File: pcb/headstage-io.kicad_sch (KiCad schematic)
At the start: 3 parts, among them J2 BTE-040-03-L-D-A, J3 BTE-040-03-L-D-A

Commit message: 1st step OEPSPN & MPN on components
- still missing new codes to be emitted
- project/schematic/components not tunned with Jon's project at this date
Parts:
- J2, J3: MPN (none) -> BTE-040-03-L-D-A; OEPSPN (none) -> espera
- R288: MPN (none) -> RG1005P-104-B-T5; OEPSPN (none) -> OEPS020175
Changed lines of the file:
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@@
 			)
 		)
-		(property "Datasheet1" ""
+		(property "Tolerance" "0.1%"
 			(at 68.58 148.59 0)
 			(effects
@@
 			)
 		)
-		(property "Part No." ""
+		(property "MPN" "RG1005P-104-B-T5"
 			(at 68.58 148.59 0)
 			(effects
@@
 			)
 		)
-		(property "Tolerance" "0.1%"
+		(property "OEPSPN" "OEPS020175"
 			(at 68.58 148.59 0)
 			(effects
@@
 			)
 		)
-		(property "Datasheet1" ""
-			(at 194.31 92.71 0)
-			(effects
-				(font
-					(size 1.27 1.27)
-				)
-				(hide yes)
-			)
-		)
-		(property "Part No." ""
-			(at 194.31 92.71 0)
-			(effects
-				(font
-					(size 1.27 1.27)
-				)
-				(hide yes)
-			)
-		)
 		(property "Tolerance" ""
 			(at 194.31 92.71 0)
@@
 					(size 1.27 1.27)
 				)
+			)
+		)
+		(property "OEPSPN" "espera"
+			(at 194.31 92.71 0)
+			(effects
+				(font
+					(size 1.27 1.27)
+				)
+				(hide yes)
+			)
+		)
+		(property "MPN" "BTE-040-03-L-D-A"
+			(at 194.31 92.71 0)
+			(effects
+				(font
+					(size 1.27 1.27)
+				)
+				(hide yes)
 			)
 		)
@@
 			)
 		)
-		(property "Datasheet1" ""
-			(at 88.9 92.71 0)
-			(effects
-				(font
-					(size 1.27 1.27)
-				)
-				(hide yes)
-			)
-		)
-		(property "Part No." ""
-			(at 88.9 92.71 0)
-			(effects
-				(font
-					(size 1.27 1.27)
-				)
-				(hide yes)
-			)
-		)
 		(property "Tolerance" ""
 			(at 88.9 92.71 0)
@@
 			)
 		)
+		(property "OEPSPN" "espera"
+			(at 88.9 92.71 0)
+			(effects
+				(font
+					(size 1.27 1.27)
+				)
+				(hide yes)
+			)
+		)
+		(property "MPN" "BTE-040-03-L-D-A"
+			(at 88.9 92.71 0)
+			(effects
+				(font
+					(size 1.27 1.27)
+				)
+				(hide yes)
+			)
+		)

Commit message: all OEPSPN
- all components with OEPSPN completed
- this Project Fork version not tunned with Project Main Branch
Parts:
- J2, J3: OEPSPN espera -> OEPS070103
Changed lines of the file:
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@@
 			)
 		)
-		(property "OEPSPN" "espera"
+		(property "OEPSPN" "OEPS070103"
 			(at 194.31 92.71 0)
 			(effects
@@
 			)
 		)
-		(property "OEPSPN" "espera"
-			(at 88.9 92.71 0)
-			(effects
+		(property "OEPSPN" "OEPS070103"
+			(at 88.9 92.71 0)
+			(effects

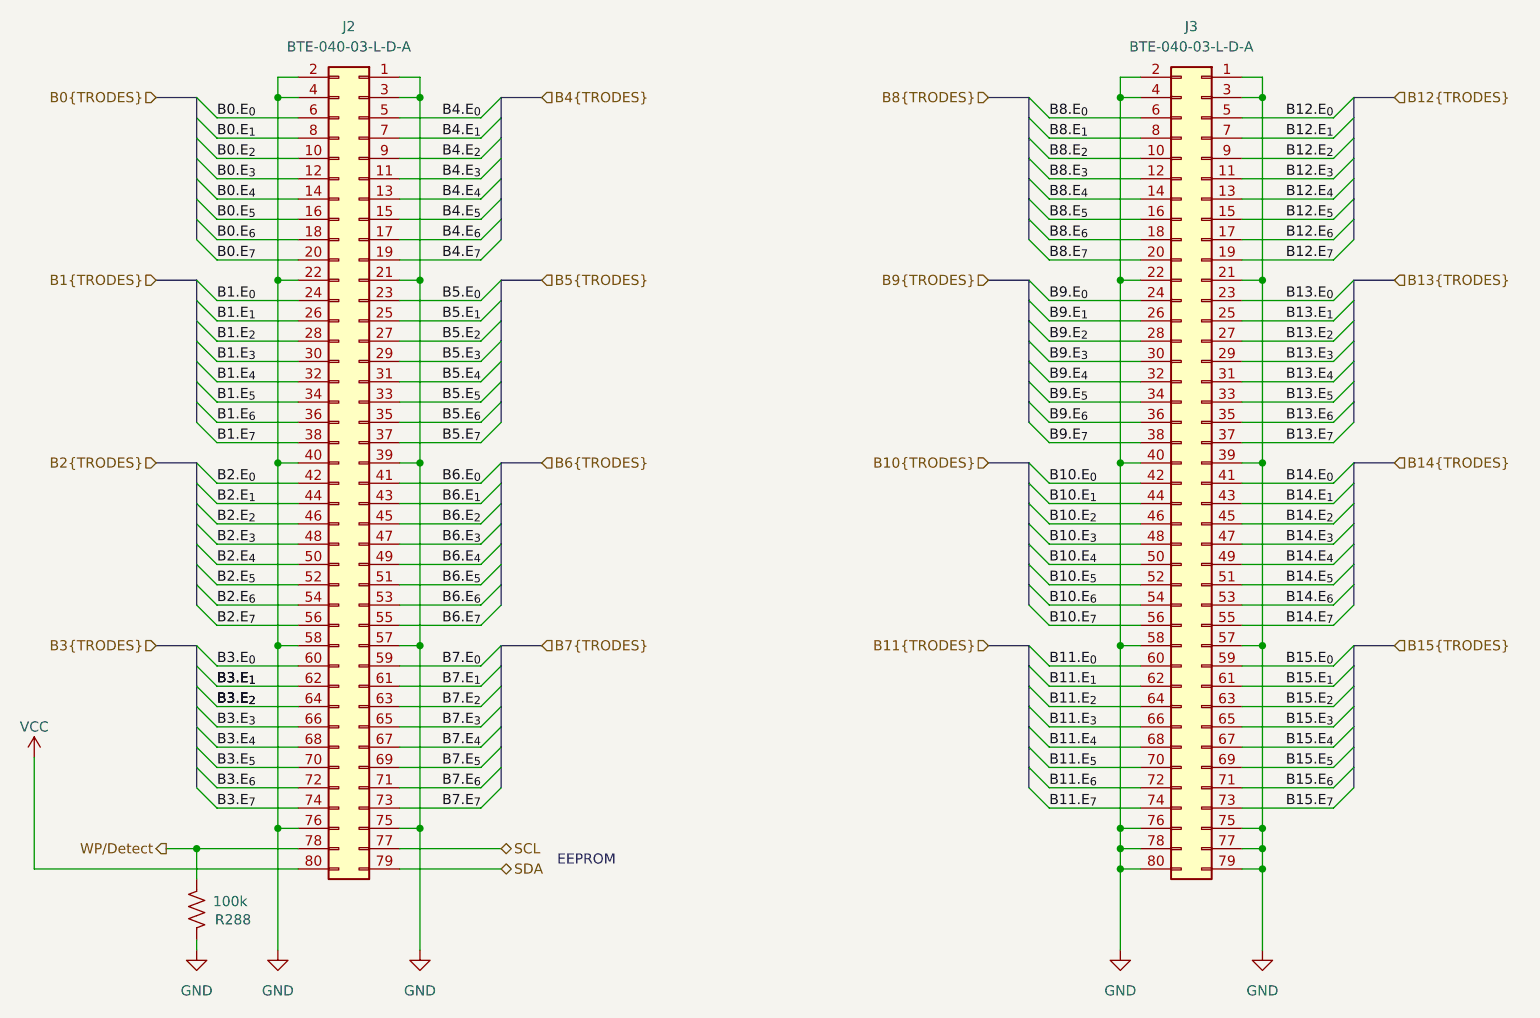
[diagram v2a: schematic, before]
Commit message: tunned with Main branch
- OEPSPN & MPN already on components
- missing 4 these codes
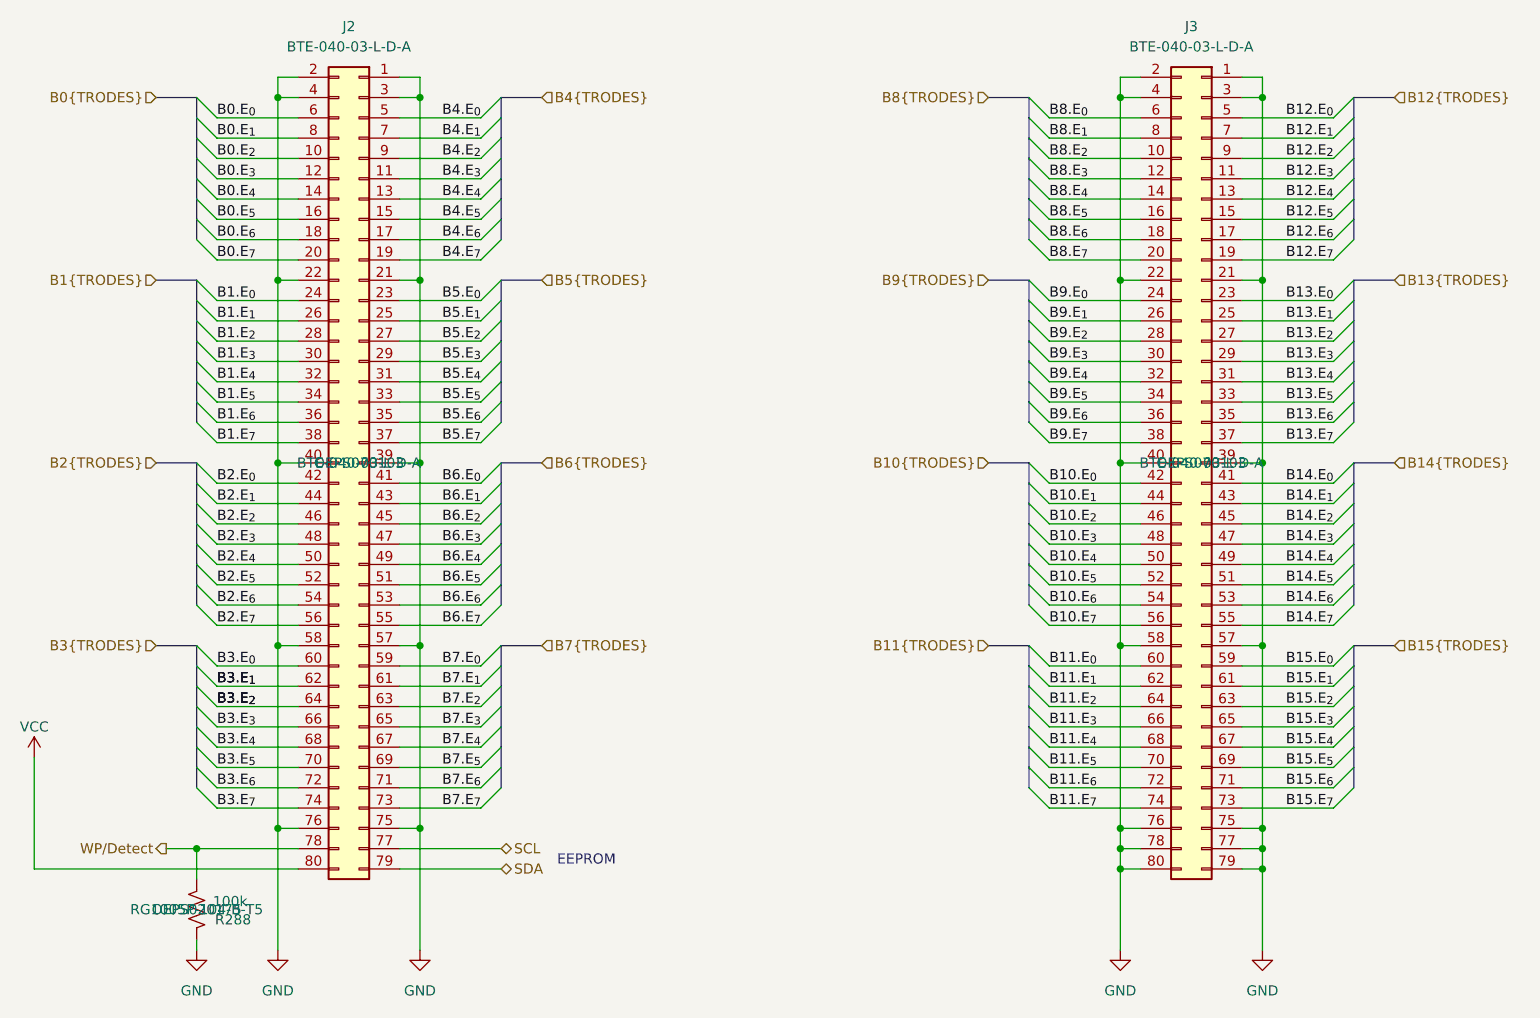
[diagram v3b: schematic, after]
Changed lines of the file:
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@@
+			)
+		)
+		(property "Datasheet1" ""
+			(at 68.58 148.59 0)
+			(effects
+				(font
+					(size 1.27 1.27)
+				)
+				(hide yes)
+			)
+		)
+		(property "Part No." ""
+			(at 68.58 148.59 0)
+			(effects
+				(font
+					(size 1.27 1.27)
+				)
+				(hide yes)
 			)
 		)
@@
 					(size 1.27 1.27)
 				)
-				(hide yes)
 			)
 		)
@@
 					(size 1.27 1.27)
 				)
-				(hide yes)
 			)
 		)
@@
 			)
 		)
+		(property "Datasheet1" ""
+			(at 194.31 92.71 0)
+			(effects
+				(font
+					(size 1.27 1.27)
+				)
+				(hide yes)
+			)
+		)
+		(property "Part No." ""
+			(at 194.31 92.71 0)
+			(effects
+				(font
+					(size 1.27 1.27)
+				)
+				(hide yes)
+			)
+		)
 		(property "Tolerance" ""
 			(at 194.31 92.71 0)
@@
 			)
 		)
+		(property "MPN" "BTE-040-03-L-D-A"
+			(at 194.31 92.71 0)
+			(effects
+				(font
+					(size 1.27 1.27)
+				)
+			)
+		)
 		(property "OEPSPN" "OEPS070103"
 			(at 194.31 92.71 0)
@@
 					(size 1.27 1.27)
 				)
-				(hide yes)
-			)
-		)
-		(property "MPN" "BTE-040-03-L-D-A"
-			(at 194.31 92.71 0)
-			(effects
-				(font
-					(size 1.27 1.27)
-				)
-				(hide yes)
 			)
 		)
@@
 			)
 		)
+		(property "Datasheet1" ""
+			(at 88.9 92.71 0)
+			(effects
+				(font
+					(size 1.27 1.27)
+				)
+				(hide yes)
+			)
+		)
+		(property "Part No." ""
+			(at 88.9 92.71 0)
+			(effects
+				(font
+					(size 1.27 1.27)
+				)
+				(hide yes)
+			)
+		)
 		(property "Tolerance" ""
 			(at 88.9 92.71 0)
@@
 			)
 		)
+		(property "MPN" "BTE-040-03-L-D-A"
+			(at 88.9 92.71 0)
+			(effects
+				(font
+					(size 1.27 1.27)
+				)
+			)
+		)
 		(property "OEPSPN" "OEPS070103"
 			(at 88.9 92.71 0)
@@
 					(size 1.27 1.27)
 				)
-				(hide yes)
-			)
-		)
-		(property "MPN" "BTE-040-03-L-D-A"
-			(at 88.9 92.71 0)
-			(effects
-				(font
-					(size 1.27 1.27)
-				)
-				(hide yes)
-			)
-		)
+			)
+		)
